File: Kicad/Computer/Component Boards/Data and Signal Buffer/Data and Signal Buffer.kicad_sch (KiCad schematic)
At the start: 10 parts, among them IC1 SN74ABT245BDBR, IC2 SN74ABT245BDBR, IC5 AP7365-33WG-7, J2 Conn_02x20_Counter_Clockwise

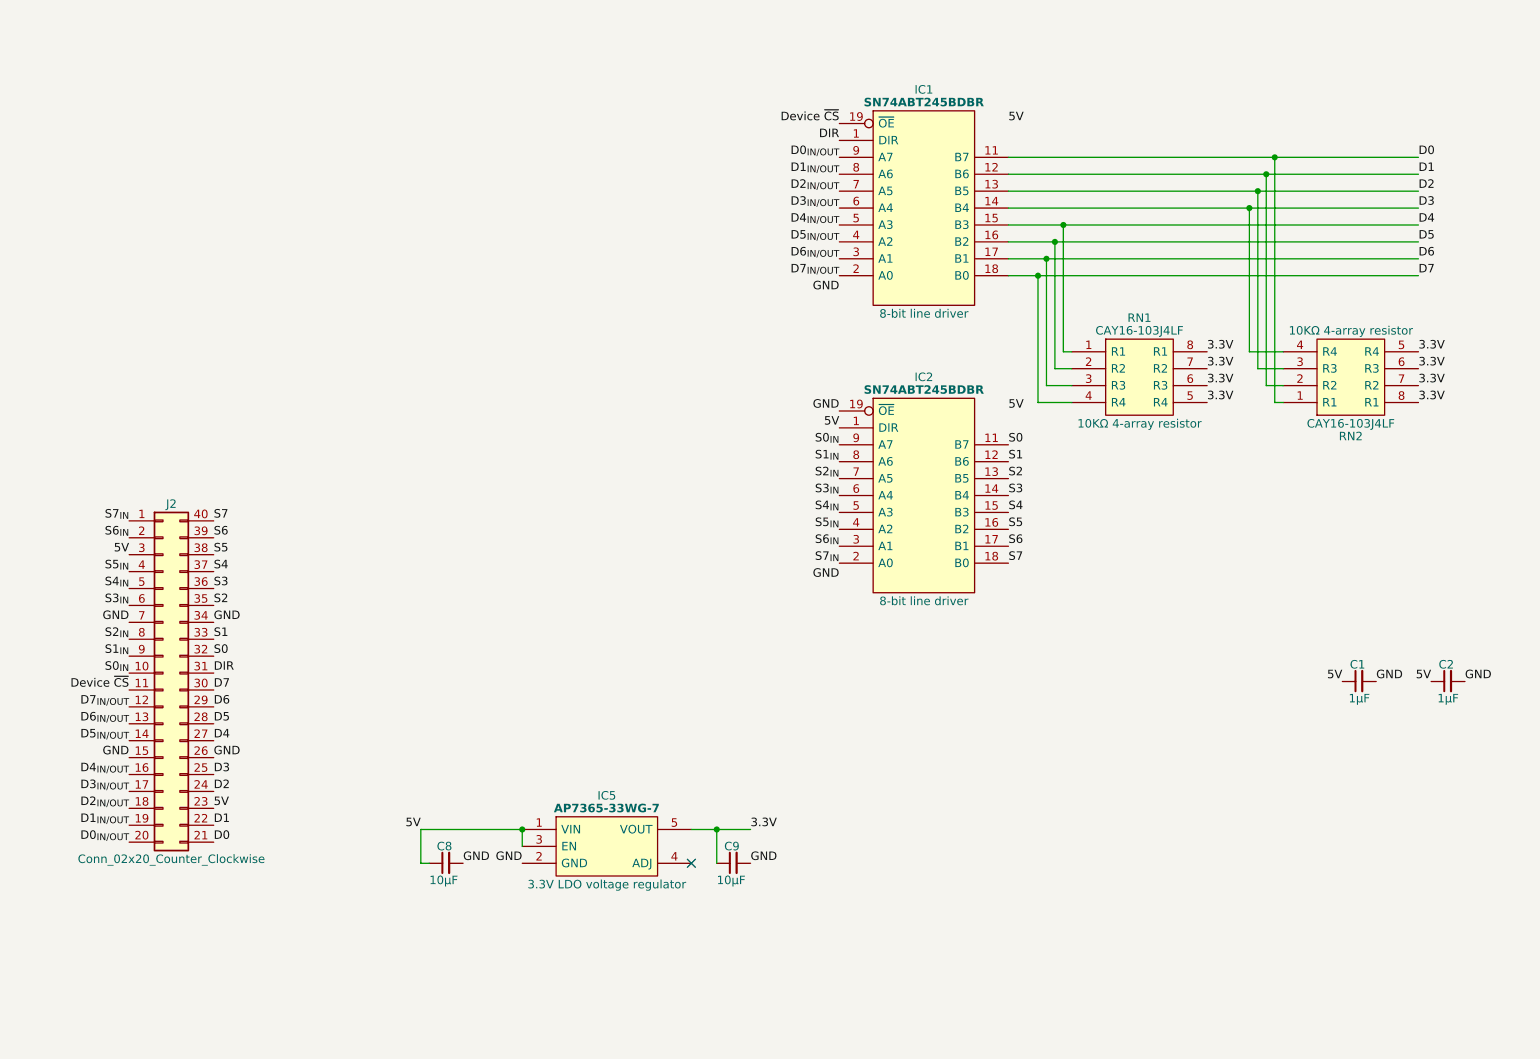
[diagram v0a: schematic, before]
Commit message: Updated the Signal Buffer to be a Data and Signal Buffer.
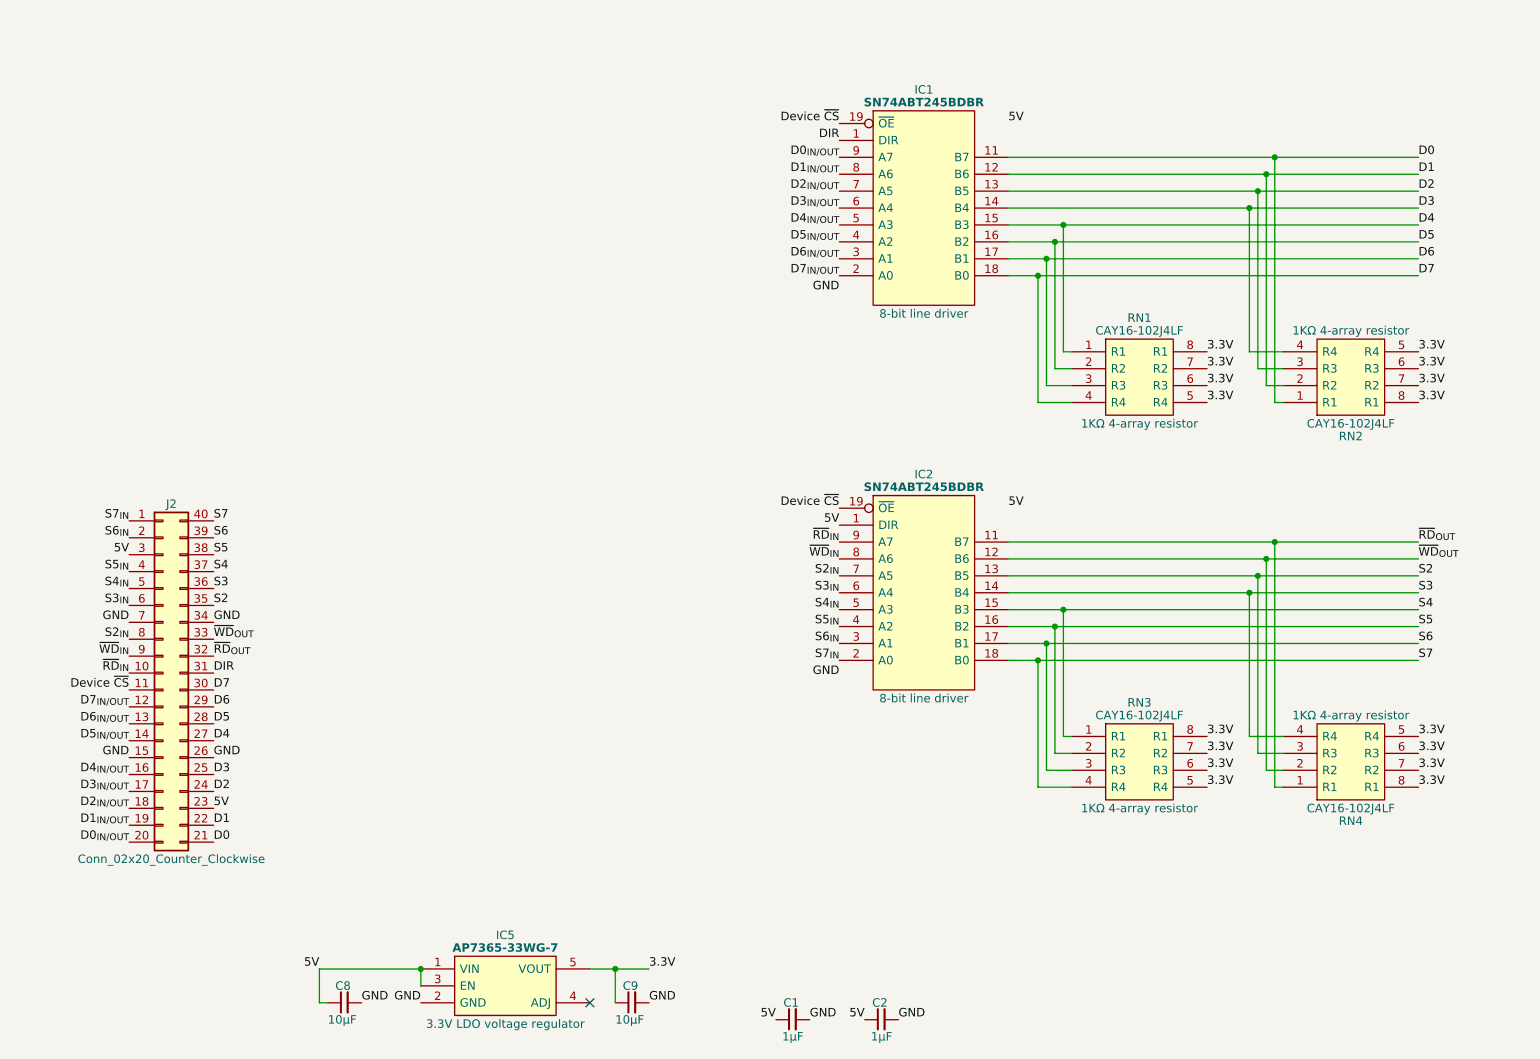
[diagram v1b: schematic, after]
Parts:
- added RN3, RN4: CAY16-102J4LF, SamacSys_Parts:CAY16-J4, symbol Bourns:CAY16-102J4LF
- RN1, RN2: value CAY16-103J4LF -> CAY16-102J4LF; symbol Bourns:CAY16-103J4LF -> Bourns:CAY16-102J4LF; Manufacturer_Part_Number CAY16-103J4LF -> CAY16-102J4LF; Mouser Part Number 652-CAY16-103J4LF -> 652-CAY16-102J4LF; Silkscreen 10KΩ -> 1KΩ
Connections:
- net 3.3V: now also RN3.5 (R4), RN3.6 (R3), RN3.7 (R2), RN3.8 (R1), RN4.5 (R4), RN4.6 (R3), RN4.7 (R2), RN4.8 (R1)
- net Device ~{CS}: now also IC2.19 (~{OE})
- net GND: no longer IC2.19 (~{OE})
- net S2: now also RN4.3 (R3)
- net S3: now also RN4.4 (R4)
- net S4: now also RN3.1 (R1)
- net S5: now also RN3.2 (R2)
- net S6: now also RN3.3 (R3)
- net S7: now also RN3.4 (R4)
- net S0 renamed ~{RD}_{OUT}
- net ~{RD}_{OUT}: now also RN4.1 (R1)
- net S0_{IN} renamed ~{RD}_{IN}
- net S1 renamed ~{WD}_{OUT}
- net ~{WD}_{OUT}: now also RN4.2 (R2)
- net S1_{IN} renamed ~{WD}_{IN}
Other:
- moved on the sheet: C1, C2, C8, C9, IC2, IC5

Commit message: Standardising DIP board layouts.
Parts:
- J2: footprint SamacSys_Parts:DIP-40_Board_W15.24mm -> (none)
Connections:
- net D4: now also J2.26 (Pin_26); no longer J2.27 (Pin_27)
- net D5_{IN/OUT}: now also J2.15 (Pin_15); no longer J2.14 (Pin_14)
- net GND: now also J2.14 (Pin_14), J2.27 (Pin_27); no longer J2.15 (Pin_15), J2.26 (Pin_26)
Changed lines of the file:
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@@
     (effects (font (size 1.27 1.27)) (justify left bottom))
   )
-  (label "D5_{IN{slash}OUT}" (at 45.085 143.51 180) (fields_autoplaced)
+  (label "D5_{IN{slash}OUT}" (at 45.085 146.05 180) (fields_autoplaced)
     (effects (font (size 1.27 1.27)) (justify right bottom))
   )
@@
     (effects (font (size 1.27 1.27)) (justify left bottom))
   )
-  (label "D4" (at 57.785 143.51 0) (fields_autoplaced)
+  (label "D4" (at 57.785 146.05 0) (fields_autoplaced)
     (effects (font (size 1.27 1.27)) (justify left bottom))
   )
@@
     (effects (font (size 1.27 1.27)) (justify right bottom))
   )
-  (label "GND" (at 57.785 146.05 0) (fields_autoplaced)
+  (label "GND" (at 57.785 143.51 0) (fields_autoplaced)
     (effects (font (size 1.27 1.27)) (justify left bottom))
   )
@@
     (effects (font (size 1.27 1.27)) (justify left bottom))
   )
-  (label "GND" (at 45.085 146.05 180) (fields_autoplaced)
+  (label "GND" (at 45.085 143.51 180) (fields_autoplaced)
     (effects (font (size 1.27 1.27)) (justify right bottom))
   )
@@
     (pin "8")
     (instances
-      (project "Signal Buffer"
+      (project "Data and Signal Buffer"
         (path "/337b5f72-8be1-4121-9dc6-479b565482b2"
           (reference "RN2") (unit 1)
@@
     (pin "2")
     (instances
-      (project "Signal Buffer"
+      (project "Data and Signal Buffer"
         (path "/337b5f72-8be1-4121-9dc6-479b565482b2"
           (reference "C1") (unit 1)
@@
     (pin "9")
     (instances
-      (project "Signal Buffer"
+      (project "Data and Signal Buffer"
         (path "/337b5f72-8be1-4121-9dc6-479b565482b2"
           (reference "IC1") (unit 1)
@@
     (pin "8")
     (instances
-      (project "Signal Buffer"
+      (project "Data and Signal Buffer"
         (path "/337b5f72-8be1-4121-9dc6-479b565482b2"
           (reference "RN4") (unit 1)
@@
     (pin "8")
     (instances
-      (project "Signal Buffer"
+      (project "Data and Signal Buffer"
         (path "/337b5f72-8be1-4121-9dc6-479b565482b2"
           (reference "RN3") (unit 1)
@@
     (pin "2")
     (instances
-      (project "Signal Buffer"
+      (project "Data and Signal Buffer"
         (path "/337b5f72-8be1-4121-9dc6-479b565482b2"
           (reference "C8") (unit 1)
@@
     (pin "9")
     (instances
-      (project "Signal Buffer"
+      (project "Data and Signal Buffer"
         (path "/337b5f72-8be1-4121-9dc6-479b565482b2"
           (reference "IC2") (unit 1)
@@
     (pin "8")
     (instances
-      (project "Signal Buffer"
+      (project "Data and Signal Buffer"
         (path "/337b5f72-8be1-4121-9dc6-479b565482b2"
           (reference "RN1") (unit 1)
@@
     (pin "5")
     (instances
-      (project "Signal Buffer"
+      (project "Data and Signal Buffer"
         (path "/337b5f72-8be1-4121-9dc6-479b565482b2"
           (reference "IC5") (unit 1)
@@
     (pin "2")
     (instances
-      (project "Signal Buffer"
+      (project "Data and Signal Buffer"
         (path "/337b5f72-8be1-4121-9dc6-479b565482b2"
           (reference "C2") (unit 1)
@@
     (pin "2")
     (instances
-      (project "Signal Buffer"
+      (project "Data and Signal Buffer"
         (path "/337b5f72-8be1-4121-9dc6-479b565482b2"
           (reference "C9") (unit 1)
@@
       (effects (font (size 1.27 1.27)))
     )
-    (property "Footprint" "SamacSys_Parts:DIP-40_Board_W15.24mm" (at 50.165 133.35 0)
+    (property "Footprint" "" (at 50.165 133.35 0)
       (effects (font (size 1.27 1.27)) hide)
     )
@@
     (pin "9")
     (instances
-      (project "Signal Buffer"
+      (project "Data and Signal Buffer"
         (path "/337b5f72-8be1-4121-9dc6-479b565482b2"
           (reference "J2") (unit 1)

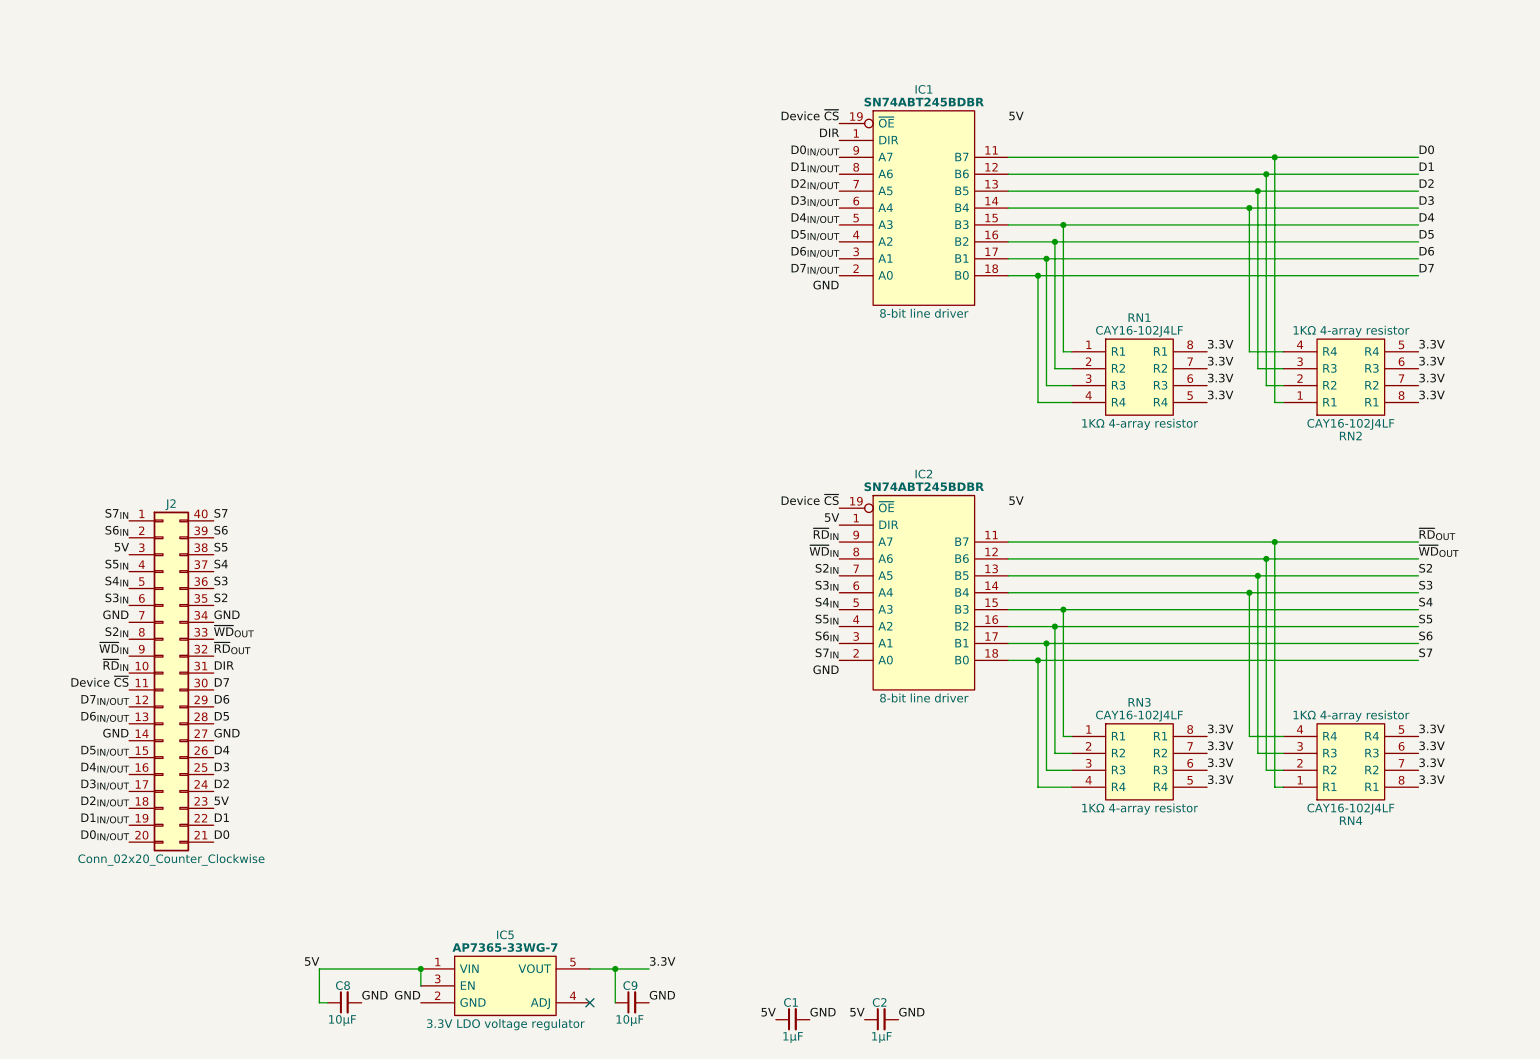
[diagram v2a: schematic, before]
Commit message: Cleaned up Data and Signal Buffer.
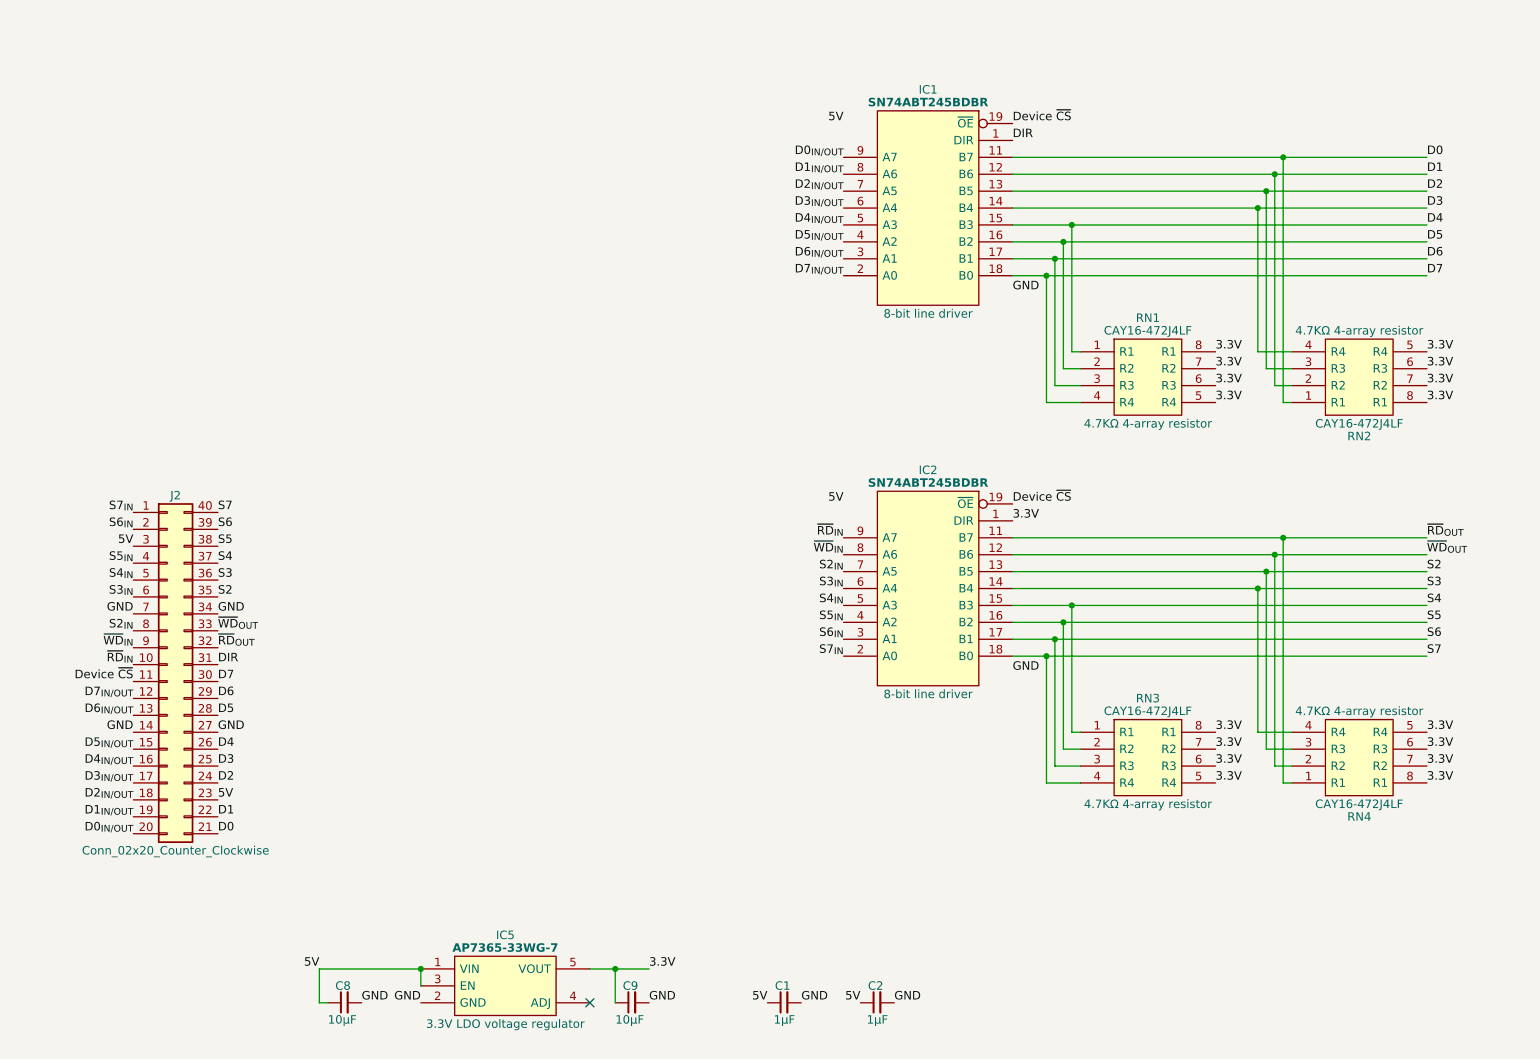
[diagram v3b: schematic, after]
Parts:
- J2: footprint (none) -> SamacSys_Parts:DIP-40_Board_W15.24mm
- RN1, RN2, RN3, RN4: value CAY16-102J4LF -> CAY16-472J4LF; footprint SamacSys_Parts:CAY16-J4 -> CAY16472J4LF; symbol Bourns:CAY16-102J4LF -> Bourns:CAY16-472J4LF; Manufacturer_Part_Number CAY16-102J4LF -> CAY16-472J4LF; Mouser Part Number 652-CAY16-102J4LF -> 652-CAY16-472J4LF; Silkscreen 1KΩ -> 4.7KΩ
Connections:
- net 3.3V: now also IC2.1 (DIR)
- net 5V: no longer IC2.1 (DIR)
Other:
- moved on the sheet: C1, C2, IC1, IC2, J2, RN1, RN2, RN3, RN4

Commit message: Trying out the Paneliser again.
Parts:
- added CN1, CN2, CN3, CN4: CA0612KRX7R9BB100, SamacSys_Parts:CA0612KRX7R9BB100, symbol Yageo:CA0612KRX7R9BB100
- added RN5, RN6, RN7, RN8: CAY16-200J4LF, SamacSys_Parts:CAY16-F4, symbol Bourns:CAY16-200J4LF
- RN1, RN2, RN3, RN4: value CAY16-472J4LF -> CAY16-103J4LF; footprint CAY16472J4LF -> SamacSys_Parts:CAY16-J4; symbol Bourns:CAY16-472J4LF -> Bourns:CAY16-103J4LF; Manufacturer_Part_Number CAY16-472J4LF -> CAY16-103J4LF; Mouser Part Number 652-CAY16-472J4LF -> 652-CAY16-103J4LF; Silkscreen 4.7KΩ -> 10KΩ
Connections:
- net D0: now also RN6.8 (R1); no longer J2.21 (Pin_21)
- net D1: now also RN6.7 (R2); no longer J2.22 (Pin_22)
- net D2: now also RN6.6 (R3); no longer J2.24 (Pin_24)
- net D3: now also RN6.5 (R4); no longer J2.25 (Pin_25)
- net D4: now also RN5.8 (R1); no longer J2.26 (Pin_26)
- net D5: now also RN5.7 (R2); no longer J2.28 (Pin_28)
- net D6: now also RN5.6 (R3); no longer J2.29 (Pin_29)
- net D7: now also RN5.5 (R4); no longer J2.30 (Pin_30)
- net GND: now also CN1.5, CN1.6, CN1.7, CN1.8, CN2.5, CN2.6, CN2.7, CN2.8, CN3.5, CN3.6, CN3.7, CN3.8, CN4.5, CN4.6, CN4.7, CN4.8
- net S2: now also RN7.6 (R3); no longer J2.35 (Pin_35)
- net S3: now also RN7.5 (R4); no longer J2.36 (Pin_36)
- net S4: now also RN8.8 (R1); no longer J2.37 (Pin_37)
- net S5: now also RN8.7 (R2); no longer J2.38 (Pin_38)
- net S6: now also RN8.6 (R3); no longer J2.39 (Pin_39)
- net S7: now also RN8.5 (R4); no longer J2.40 (Pin_40)
- net ~{RD}_{OUT} renamed ~{RD}
- net ~{RD}: now also RN7.8 (R1); no longer J2.32 (Pin_32)
- net ~{WD}_{OUT} renamed ~{WD}
- net ~{WD}: now also RN7.7 (R2); no longer J2.33 (Pin_33)
- new net D0_{s}: CN2.4, J2.21 (Pin_21), RN6.1 (R1)
- new net D1_{s}: CN2.3, J2.22 (Pin_22), RN6.2 (R2)
- new net D2_{s}: CN2.2, J2.24 (Pin_24), RN6.3 (R3)
- new net D3_{s}: CN2.1, J2.25 (Pin_25), RN6.4 (R4)
- new net D4_{s}: CN1.4, J2.26 (Pin_26), RN5.1 (R1)
- new net D5_{s}: CN1.3, J2.28 (Pin_28), RN5.2 (R2)
- new net D6_{s}: CN1.2, J2.29 (Pin_29), RN5.3 (R3)
- new net D7_{s}: CN1.1, J2.30 (Pin_30), RN5.4 (R4)
- new net S2_{s}: CN3.2, J2.35 (Pin_35), RN7.3 (R3)
- new net S3_{s}: CN3.1, J2.36 (Pin_36), RN7.4 (R4)
- new net S4_{s}: CN4.4, J2.37 (Pin_37), RN8.1 (R1)
- new net S5_{s}: CN4.3, J2.38 (Pin_38), RN8.2 (R2)
- new net S6_{s}: CN4.2, J2.39 (Pin_39), RN8.3 (R3)
- new net S7_{s}: CN4.1, J2.40 (Pin_40), RN8.4 (R4)
- new net ~{RD}_{s}: CN3.4, J2.32 (Pin_32), RN7.1 (R1)
- new net ~{WD}_{s}: CN3.3, J2.33 (Pin_33), RN7.2 (R2)
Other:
- moved on the sheet: IC1, IC2, RN1, RN2, RN3, RN4
